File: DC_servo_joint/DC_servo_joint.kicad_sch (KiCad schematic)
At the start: 41 parts, among them U1 AS5600, U2 ESP32-C3-WROOM-02, U3 SP3485EN, U5 TPS563200

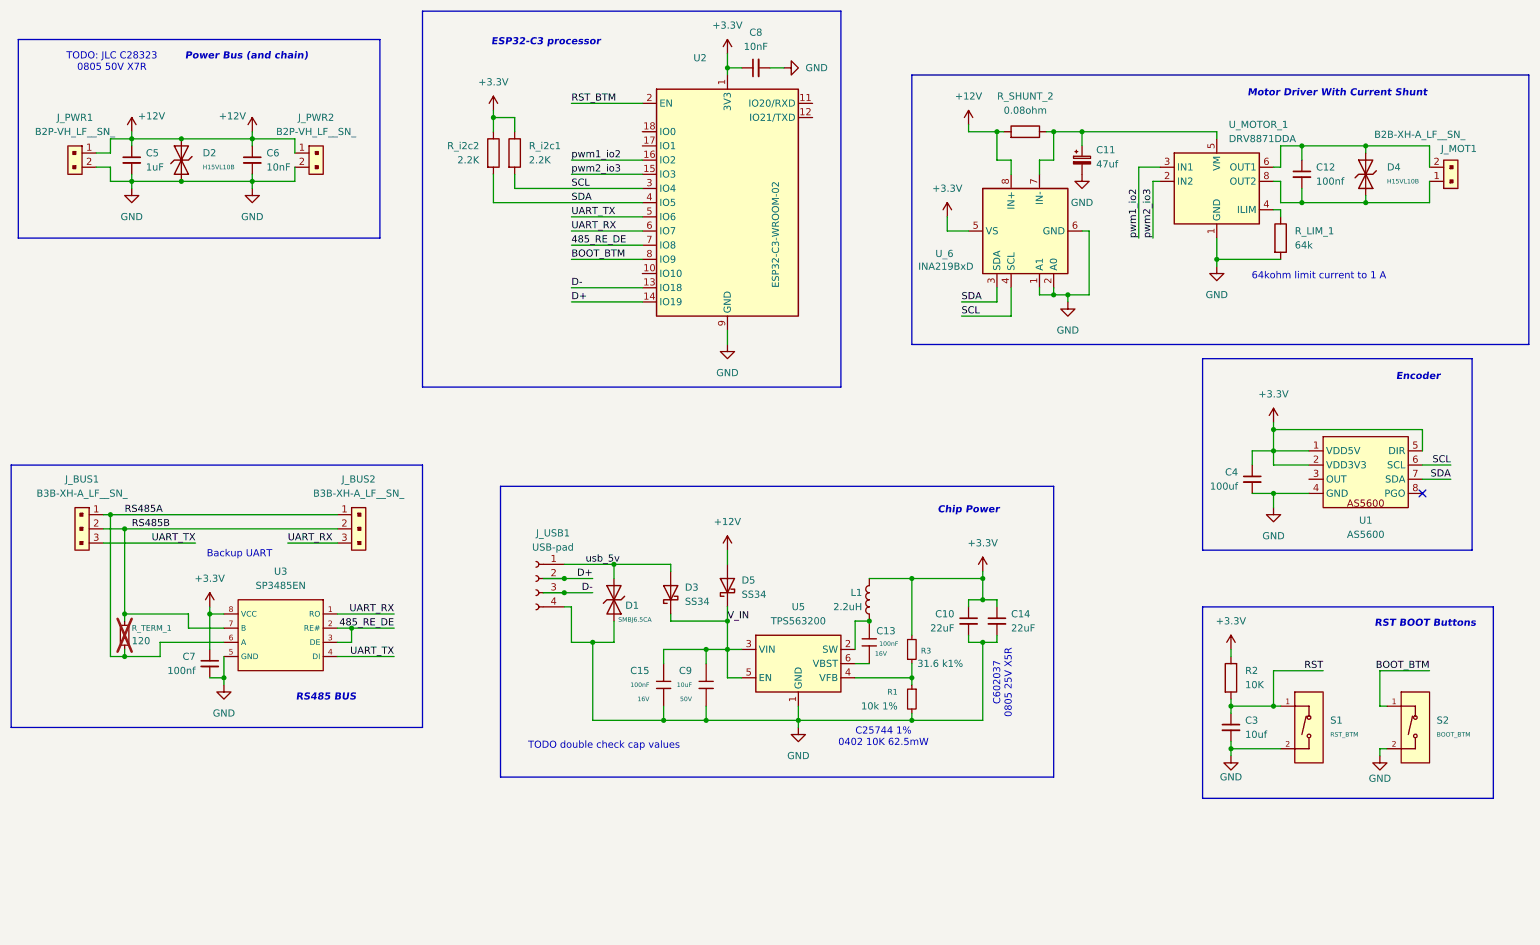
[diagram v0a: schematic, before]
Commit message: Made part selection for all caps and resistors.
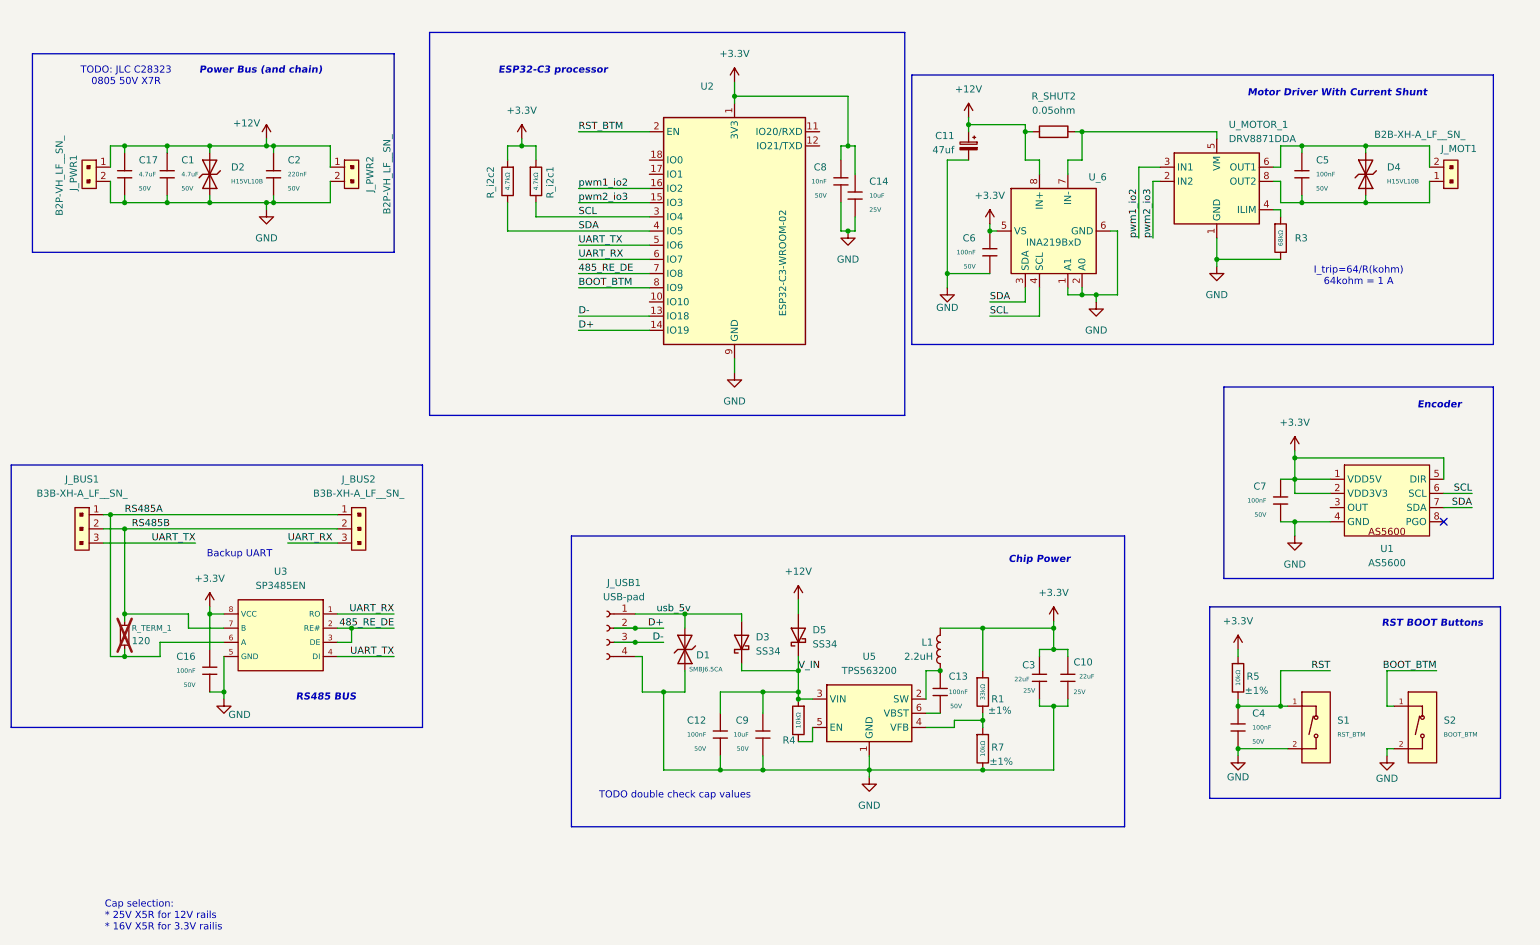
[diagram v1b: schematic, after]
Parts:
- removed C10, C14: 22uF, symbol Device:C_Small
- removed C12, C7: 100nf, symbol Device:C_Small
- removed C13, C15: 100nF, PCM_JLCPCB:C_0402, symbol PCM_JLCPCB-Capacitors:0402,100nF
- removed C3: 10uf, symbol Device:C_Small
- removed C4: 100uf, symbol Device:C_Small
- removed C5: 1uF, digikey-footprints:1206, symbol Device:C_Small
- removed C6, C8: 10nF, digikey-footprints:1206, symbol Device:C_Small
- removed C9: 10uF, PCM_JLCPCB:C_0805, symbol PCM_JLCPCB-Capacitors:0805,10uF,(2)
- removed R1: 10k 1%, symbol Device:R_Small
- removed R2: 10K, symbol Device:R
- removed R3: 31.6 k1%, symbol Device:R_Small
- removed R_LIM_1: 64k, symbol Device:R
- removed R_i2c1, R_i2c2: 2.2K, symbol Device:R
- added C1, C17: 4.7uF, PCM_JLCPCB:C_1206, symbol PCM_JLCPCB-Capacitors:1206,4.7uF
- added C10, C3: 22uF, PCM_JLCPCB:C_1206, symbol PCM_JLCPCB-Capacitors:1206,22uF,(2)
- added C12, C13, C16, C4, C6, C7: 100nF, PCM_JLCPCB:C_0603, symbol PCM_JLCPCB-Capacitors:0603,100nF
- added C14: 10uF, PCM_JLCPCB:C_0805, symbol PCM_JLCPCB-Capacitors:0805,10uF
- added C2: 220nF, PCM_JLCPCB:C_1206, symbol PCM_JLCPCB-Capacitors:1206,220nF
- added C5: 100nF, PCM_JLCPCB:C_1206, symbol PCM_JLCPCB-Capacitors:1206,100nF
- added C8: 10nF, PCM_JLCPCB:C_0603, symbol PCM_JLCPCB-Capacitors:0603,10nF
- added C9: 10uF, PCM_JLCPCB:C_1206, symbol PCM_JLCPCB-Capacitors:1206,10uF
- added R1: 33kΩ, PCM_JLCPCB:R_0402, symbol PCM_JLCPCB-Resistors:0402,33kΩ
- added R3: 68kΩ, PCM_JLCPCB:R_0805, symbol PCM_JLCPCB-Resistors:0805,68kΩ
- added R4: 10kΩ, PCM_JLCPCB:R_0603, symbol PCM_JLCPCB-Resistors:0603,10kΩ
- added R5, R7: 10kΩ, PCM_JLCPCB:R_0402, symbol PCM_JLCPCB-Resistors:0402,10kΩ
- added R_i2c1, R_i2c2: 4.7kΩ, PCM_JLCPCB:R_0402, symbol PCM_JLCPCB-Resistors:0402,4.7kΩ
- R_SHUT2: renamed from R_SHUNT_2; value 0.08ohm -> 0.05ohm; footprint (none) -> digikey-footprints:1206; JLC (none) -> C7467249; URL (none) -> https://jlcpcb.com/partdetail/FOJAN-FRM121WFR050TM/C7467249
- R_TERM_1: footprint (none) -> digikey-footprints:0805
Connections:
- net +12V: now also C11.1, C1.1, C17.1, C2.1
- net +3.3V: now also C10.1, C14.1, C16.1, C3.1, C6.1, C7.1, C8.1, R1.1, R5.1, R_i2c1.1, R_i2c2.1
- net GND: now also C1.2, C10.2, C12.2, C14.2, C16.2, C17.2, C2.2, C3.2, C4.2, C6.2, C7.2, C8.2, C9.2, R3.2, R7.2
- net RST: now also C4.1, R5.2
- net SCL: now also R_i2c1.2
- net SDA: now also R_i2c2.2
- net V_IN: now also C12.1, C9.1, R4.1; no longer U5.5 (EN)
- net at U5.4 (VFB): now also R1.2, R7.1
- net at L1.2, U5.2 (SW): now also C13.1
- net at R_SHUT2.1, U_6.7 (IN-), U_MOTOR_1.5 (VM): no longer C11.1
- net at U_MOTOR_1.4 (ILIM): now also R3.1
- net at D4.2, J_MOT1.2, U_MOTOR_1.6 (OUT1): now also C5.1
- net at D4.1, J_MOT1.1, U_MOTOR_1.8 (OUT2): now also C5.2
- net at U5.6 (VBST): now also C13.2
- new net: R4.2, U5.5 (EN)
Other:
- note added: "Cap selection: * 25V X5R for 12V rails * 16V X5R for 3.3V railis"
- note added: "I_trip=64/R(kohm) 64kohm = 1 A"
- note removed: "64kohm limit current to 1 A"
- note removed: "C25744 1% 0402 10K 62.5mW"
- note removed: "C602037 0805 25V X5R"
- moved on the sheet: C11, D1, D2, D3, D5, J_PWR1, J_PWR2, J_USB1, L1, R_SHUT2, S1, S2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

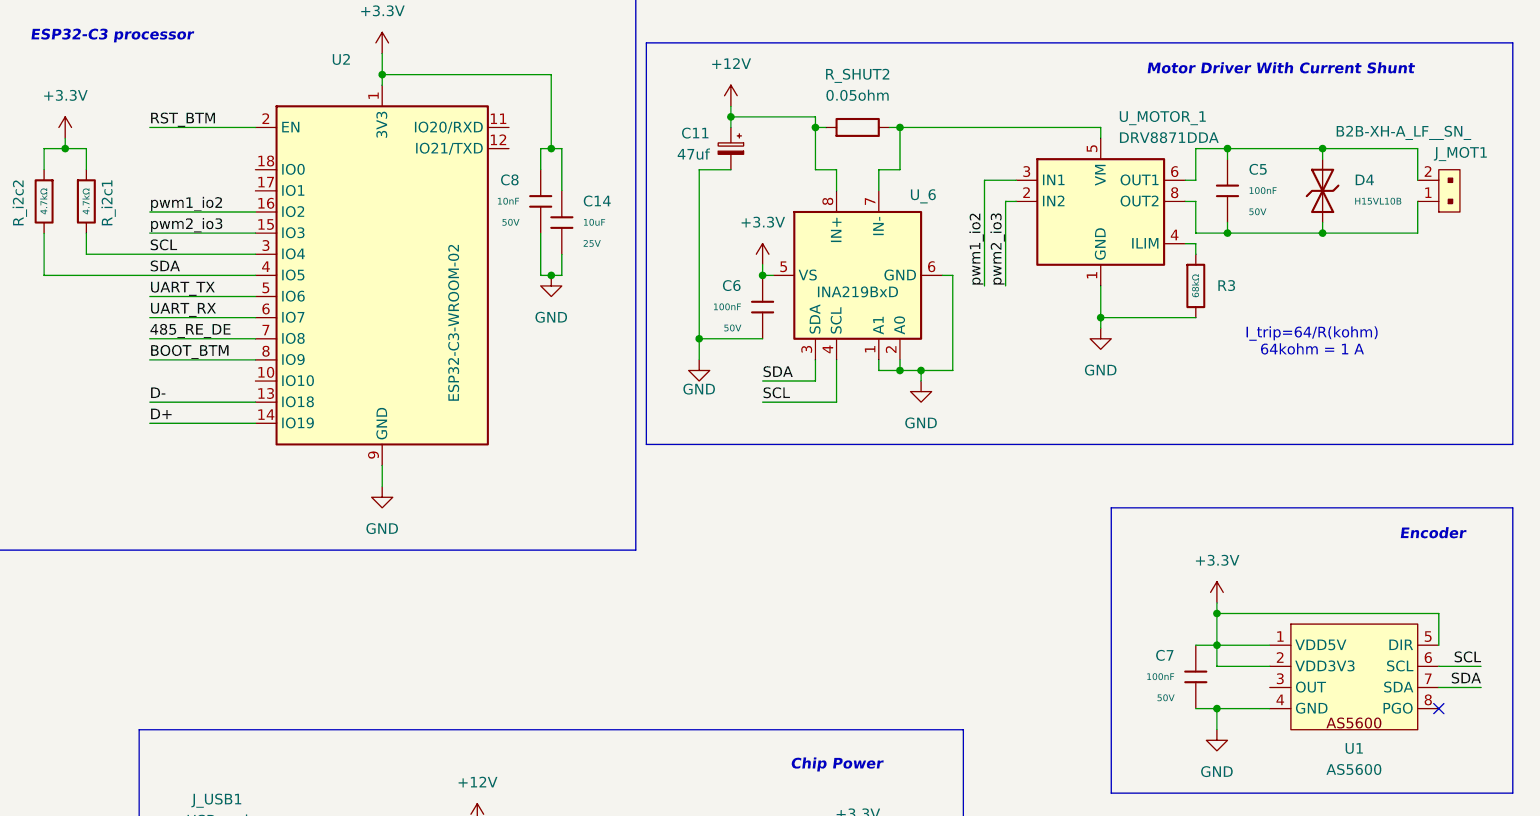
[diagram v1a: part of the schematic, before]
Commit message: Added a NTP to the system.
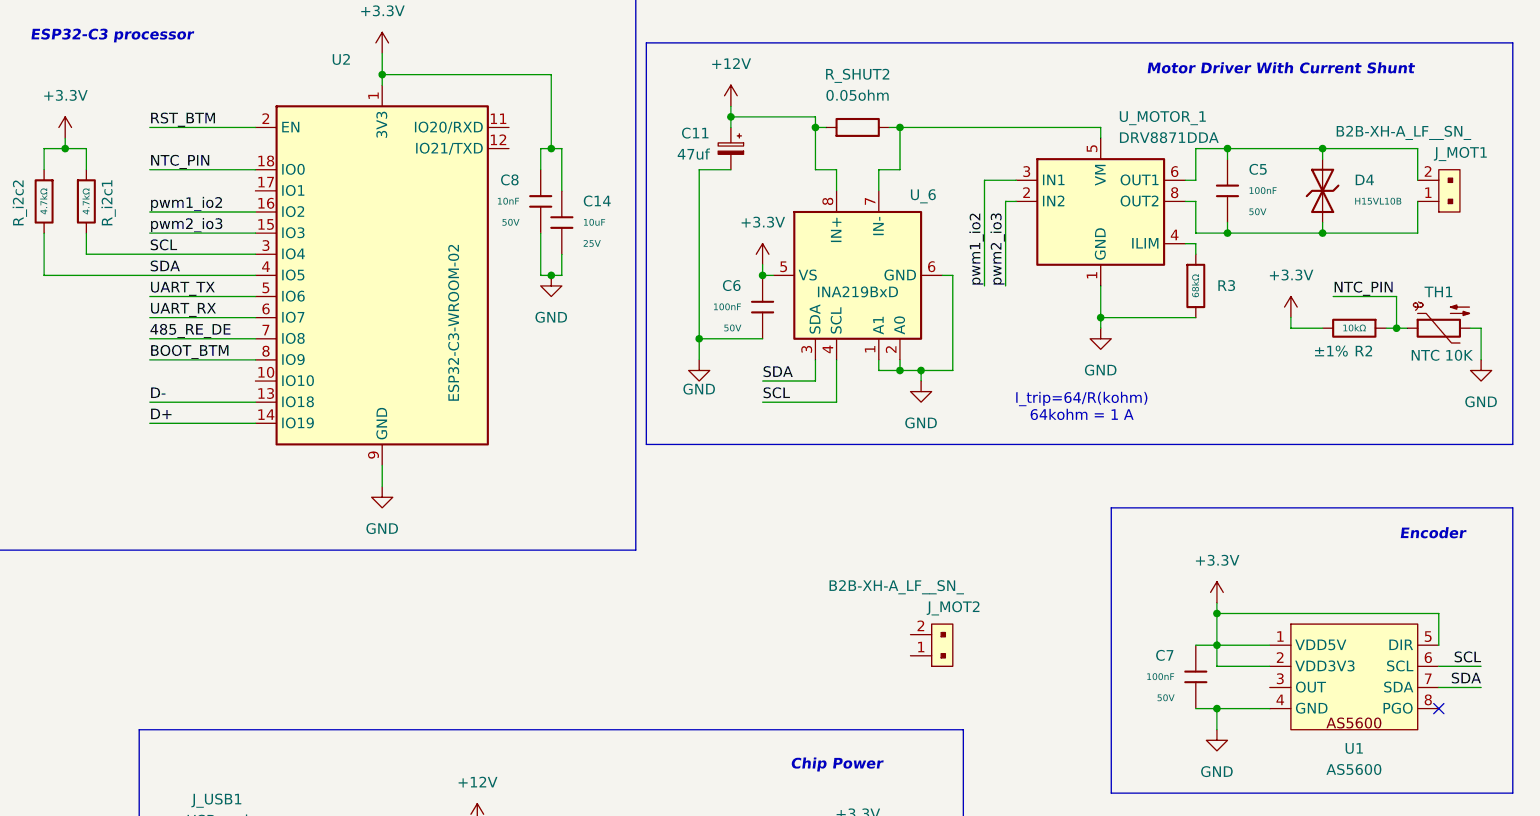
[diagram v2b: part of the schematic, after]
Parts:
- added J_MOT2: B2B-XH-A_LF__SN_, digikey-footprints:PinHeader_1x2_P2.5mm_Drill1.1mm, symbol dk_Rectangular-Connectors-Headers-Male-Pins:B2B-XH-A_LF__SN_
- added R2: 10kΩ, PCM_JLCPCB:R_0402, symbol PCM_JLCPCB-Resistors:0402,10kΩ
- added TH1: NTC 10K, Connector_JST:JST_XH_S2B-XH-A_1x02_P2.50mm_Horizontal, symbol Device:Thermistor_NTC
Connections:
- net +3.3V: now also R2.2
- net GND: now also TH1.2
- net NTC_PIN: now reaches U2.18 (IO0)
- net NTC_PIN: now also R2.1, TH1.1
